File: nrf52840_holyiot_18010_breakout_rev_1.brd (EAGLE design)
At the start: 33.8 x 25.5 mm, 22 parts, among them IC1 MMA8652FCR1, IC2 HOLYIOT_18010, J1 NO_BOM, J2 NO_BOM

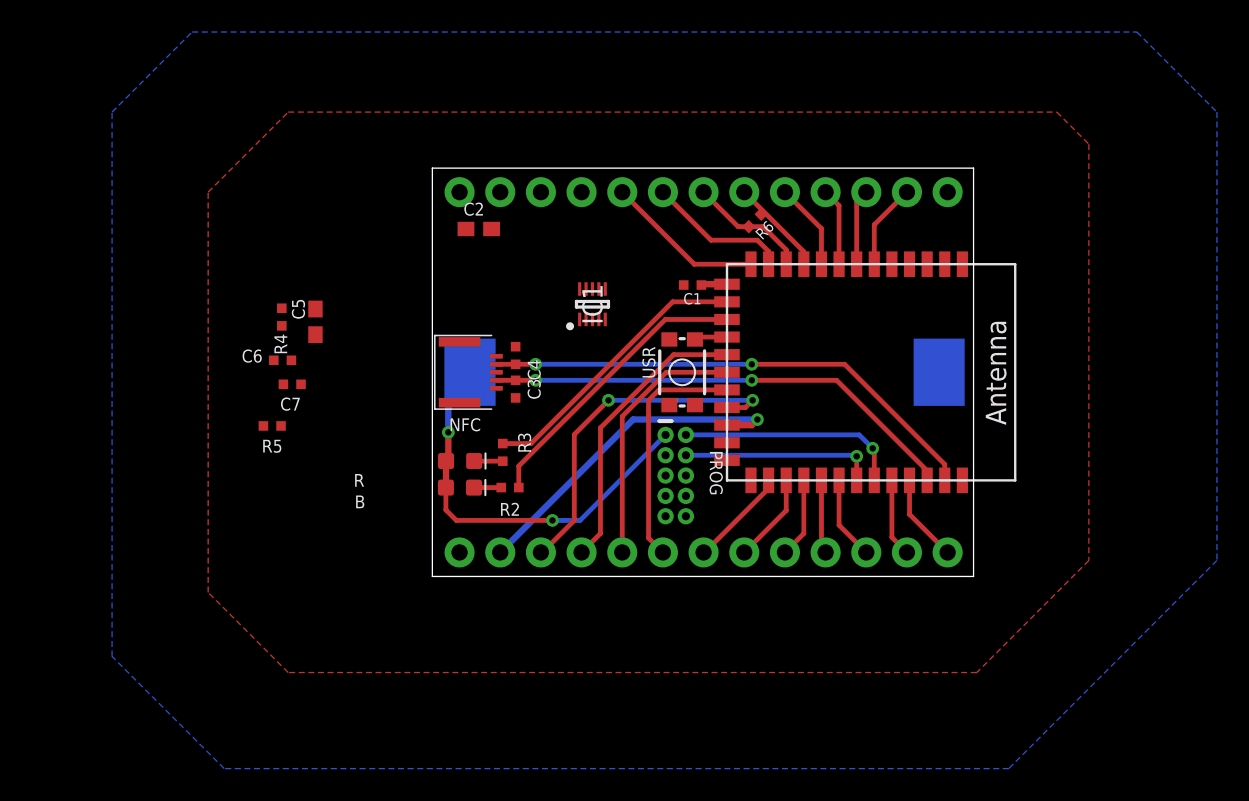
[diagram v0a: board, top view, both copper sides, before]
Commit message: added temp sensor, first draft routing done
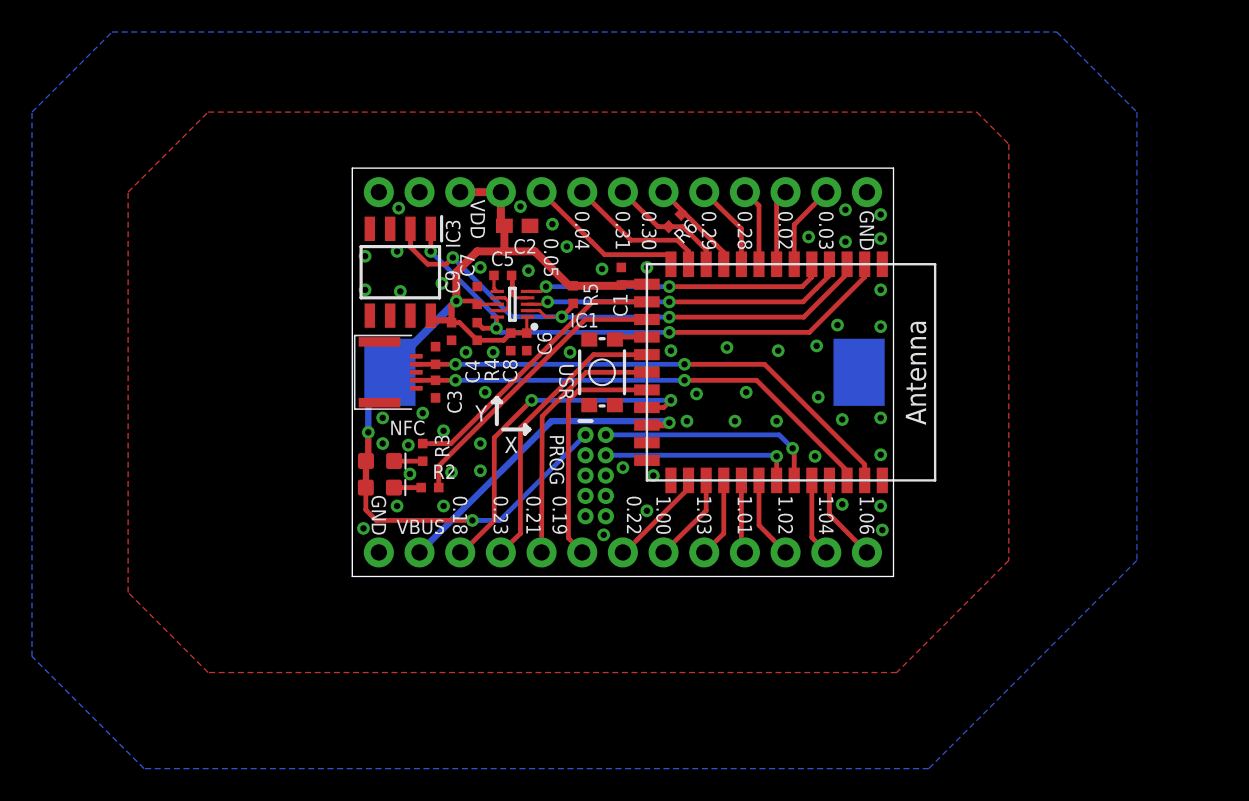
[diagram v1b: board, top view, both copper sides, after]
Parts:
- added C8: 1uF, Inventas-Passives:C0402
- added C9: 0.1uF, Inventas-Passives:C0402
- added IC3: AT30TS74-SS8M-T, Inventas-IC:SOIC127P600X175-8N
- C5: value 4.7uF -> 0.1uF; device Inventas-Passives:C0603 -> Inventas-Passives:C0402
- J1, J2: device SparkFun-Connectors:1X13 -> Inventas-Connectors:1X13_NO_SILK
- R4, R5: value 4.7k -> 1k
- moved R5 20.5 mm to (13.8, 17.6), turned to 90 degrees
- moved C6 15.3 mm to (10.9, 14.7), turned to 270 degrees
- moved C7 12.8 mm to (7.80, 17.6), turned to 90 degrees
- moved R4 12.2 mm to (7.80, 15.3), turned to 270 degrees
- moved C5 12.1 mm to (9.40, 18.8), turned to 180 degrees
- moved J1 10.2 mm to (16.9, 1.50)
- moved J2 10.2 mm to (16.9, 24.0)
- moved USR 5.00 mm to (15.6, 12.8)
- moved B1 5.00 mm to (17.0, 12.8)
- moved D1 5.00 mm to (1.72, 5.55)
- moved D2 5.00 mm to (1.73, 7.21)
- moved IC1 5.00 mm to (10.0, 17.0), turned to 180 degrees
- moved IC2 5.00 mm to (27.4, 12.8)
- moved NFC 5.00 mm to (4.00, 12.8)
- moved PROG 5.00 mm to (15.2, 6.30)
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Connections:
- removed net N$13: J2.4
- removed net N$14: J2.3
- removed net N$6: C7.2
- removed net N1: R5.1
- removed net N2: R4.1
- removed net P1.10: IC2.2
- removed net P1.11: IC2.3
- removed net P1.13: IC2.4
- removed net P1.15: IC2.5
- new net ACC_INT1: IC1.3, IC2.4
- new net ACC_INT2: IC1.5, IC2.5
- new net I2C_SCL: IC1.2, IC2.3, IC3.2, R5.1
- new net I2C_SDA: IC1.10, IC2.2, IC3.1, R4.1
- new net N$3: C5.1, IC1.4
- net GND: now also C6.2, C7.2, C8.2, C9.2, IC1.6, IC1.7, IC1.9, IC3.4, IC3.5, IC3.6, IC3.7, J2.2; no longer C6.1, C7.1
- net VDD: now also C6.1, C7.1, C8.1, C9.1, IC1.1, IC1.8, IC3.8, J2.3, J2.4; no longer C5.1, C6.2, J2.2
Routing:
- net VDD: track 27.0 -> 65.1 mm, vias 2 -> 3
- net I2C_SCL: track 0.00 -> 35.7 mm, vias 0 -> 3
- net I2C_SDA: track 0.00 -> 35.3 mm, vias 0 -> 3
- net ACC_INT1: track 0.00 -> 20.3 mm, vias 0 -> 2
- net ACC_INT2: track 0.00 -> 18.9 mm, vias 0 -> 2
- net GND: track 0.00 -> 3.01 mm, vias 0 -> 58
- net N$3: track 0.00 -> 2.25 mm
- net VBUS: track 21.5 -> 20.5 mm
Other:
- board text added: "0.02"
- board text added: "0.03"
- board text added: "0.04"
- board text added: "0.05"
- board text added: "0.18"
- board text added: "0.19"
- board text added: "0.21"
- board text added: "0.22"
- board text added: "0.23"
- board text added: "0.28"
- board text added: "0.29"
- board text added: "0.30"
- board text added: "0.31"
- board text added: "1.00"
- board text added: "1.01"
- board text added: "1.02"
- board text added: "1.03"
- board text added: "1.04"
- board text added: "1.06"
- board text added: "VBUS"
- board text added: "VDD"
- board text removed: "B"
- board text removed: "R"
- board text removed: "User button: P0.08 LED red: P0.02 LED blue: P0.03 MMA8452 SCL: P0.07 MMA8452 SDA: P0.06 MMA8452 INT1: P0.04 MMA8452 INT2: P0.05 MMA8452 addr: 0x1C"

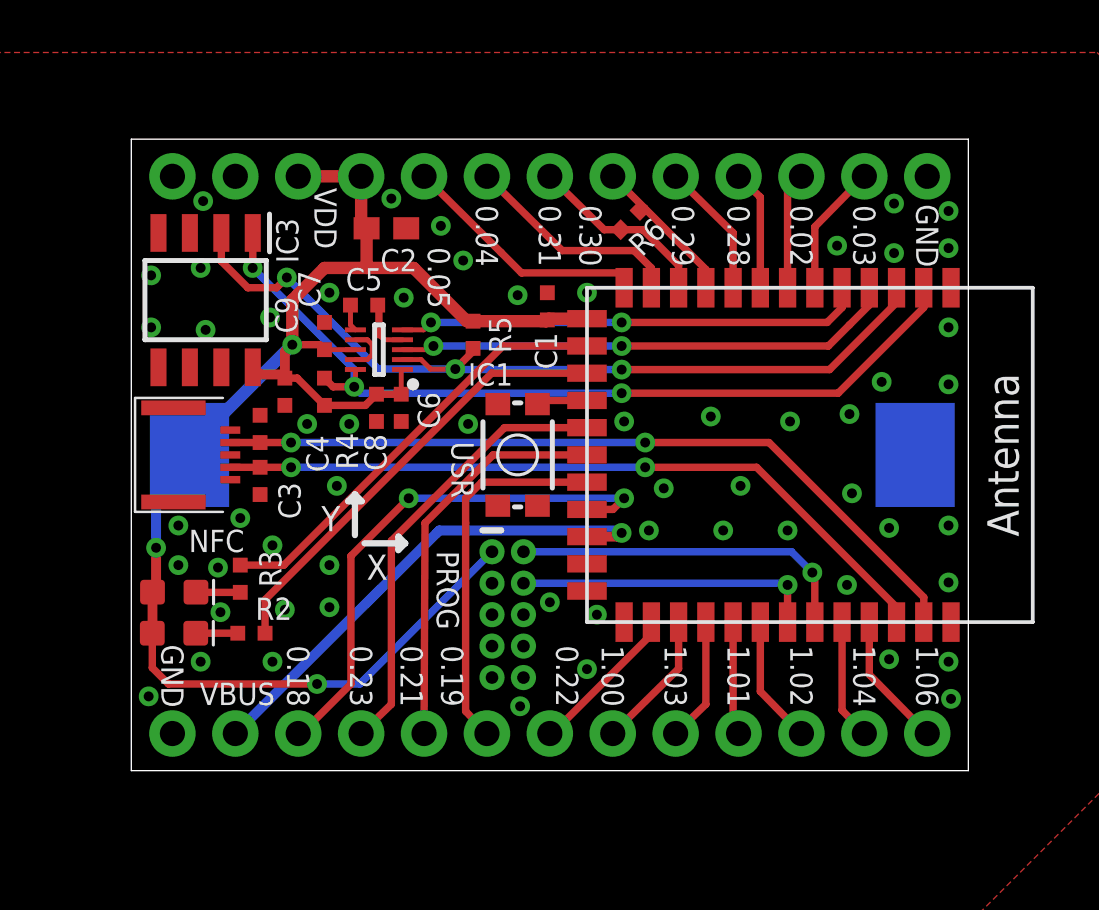
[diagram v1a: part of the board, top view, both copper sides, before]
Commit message: small fixes when adding 3D packages
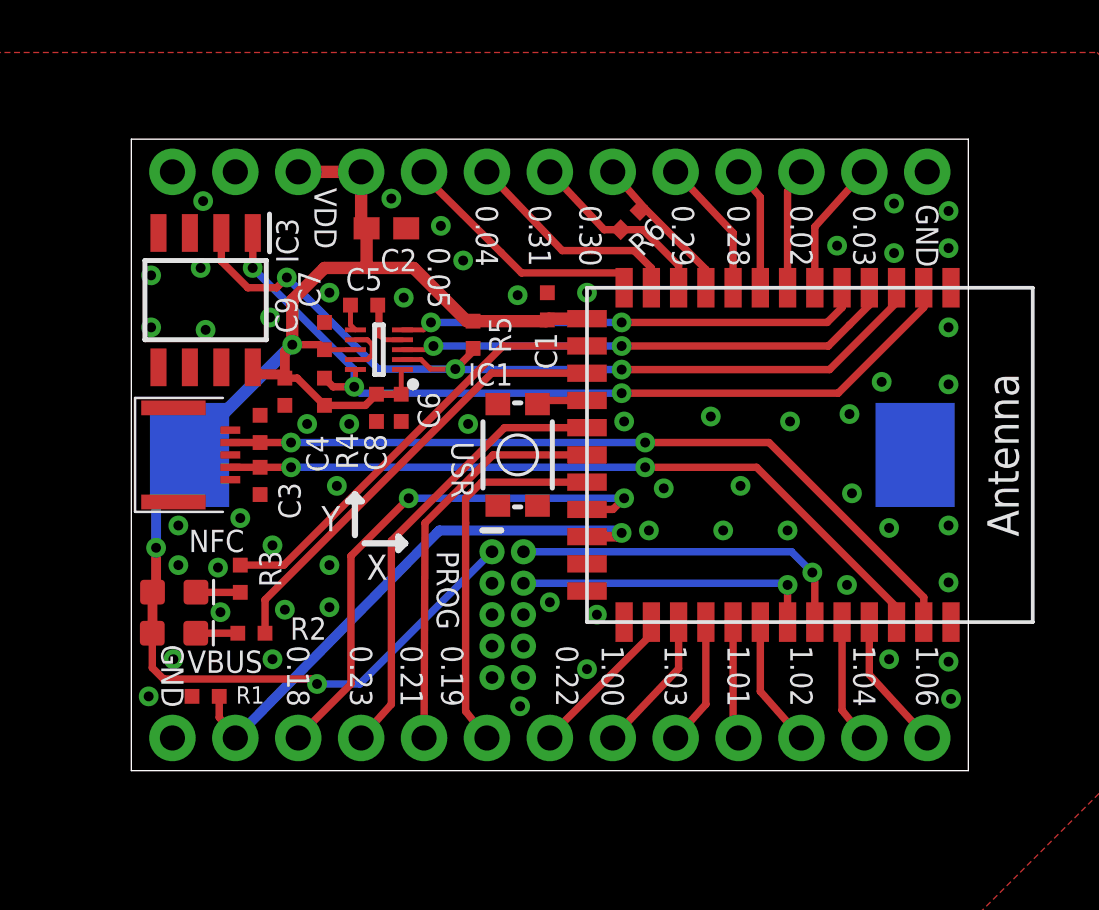
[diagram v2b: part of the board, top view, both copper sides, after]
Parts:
- added R1: 0R, Inventas-Passives:R0402
- moved J1 0.18 mm to (16.9, 1.32)
- moved J2 0.18 mm to (16.9, 24.2)
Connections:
- net GND: now also R1.1
- net VBUS: now also R1.2
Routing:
- net VBUS: track 20.5 -> 22.5 mm
